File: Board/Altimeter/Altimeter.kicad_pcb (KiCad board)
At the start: 2 copper layers, 50 x 30 mm, 63 parts, among them J1 PWRIN, J2 STLink, J3 Micro_SD_Card_Det_Hirose_DM3AT, J4 GNSS, J5 RS485, J6 ReleaseSys, SW1 SW_RESET, U1 STM32L431RBTx, U2 LPS22HB_Module, U3 ST1480AxDR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

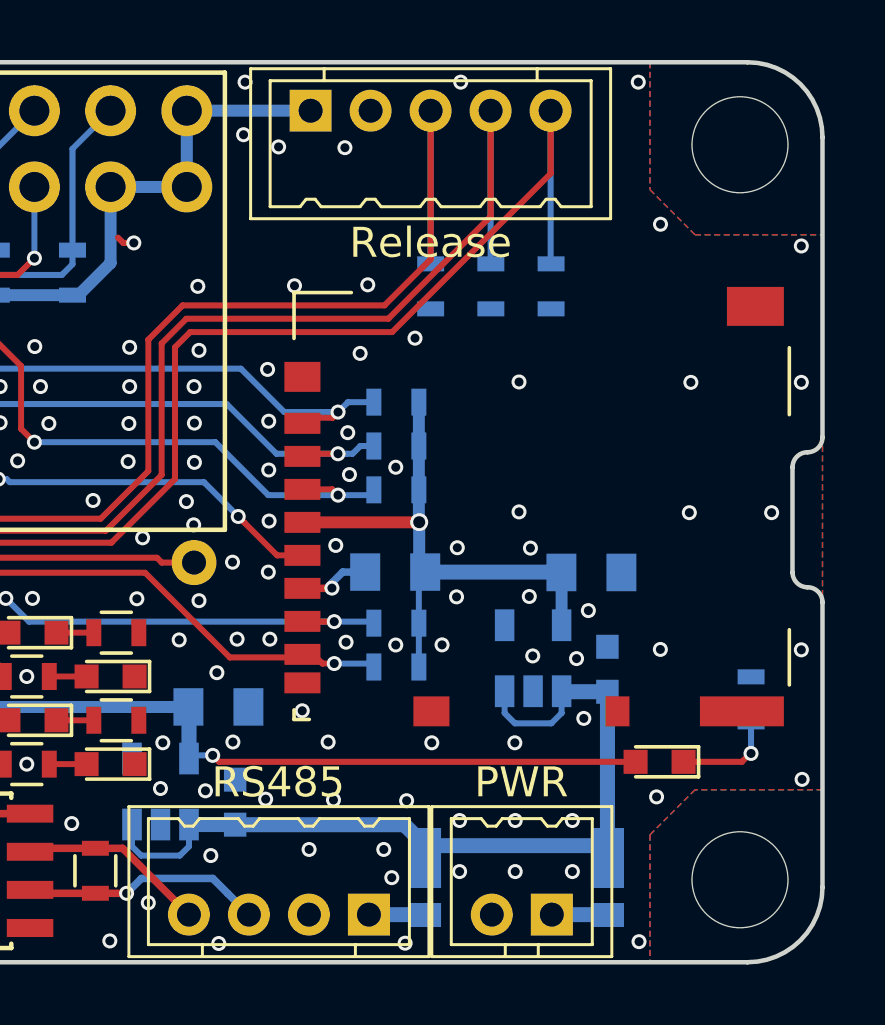
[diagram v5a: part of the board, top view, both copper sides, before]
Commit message: [Altimeter V1.2] Added another power input way at J6 and added a solder jumper to switch 3V Output / 6V Input.
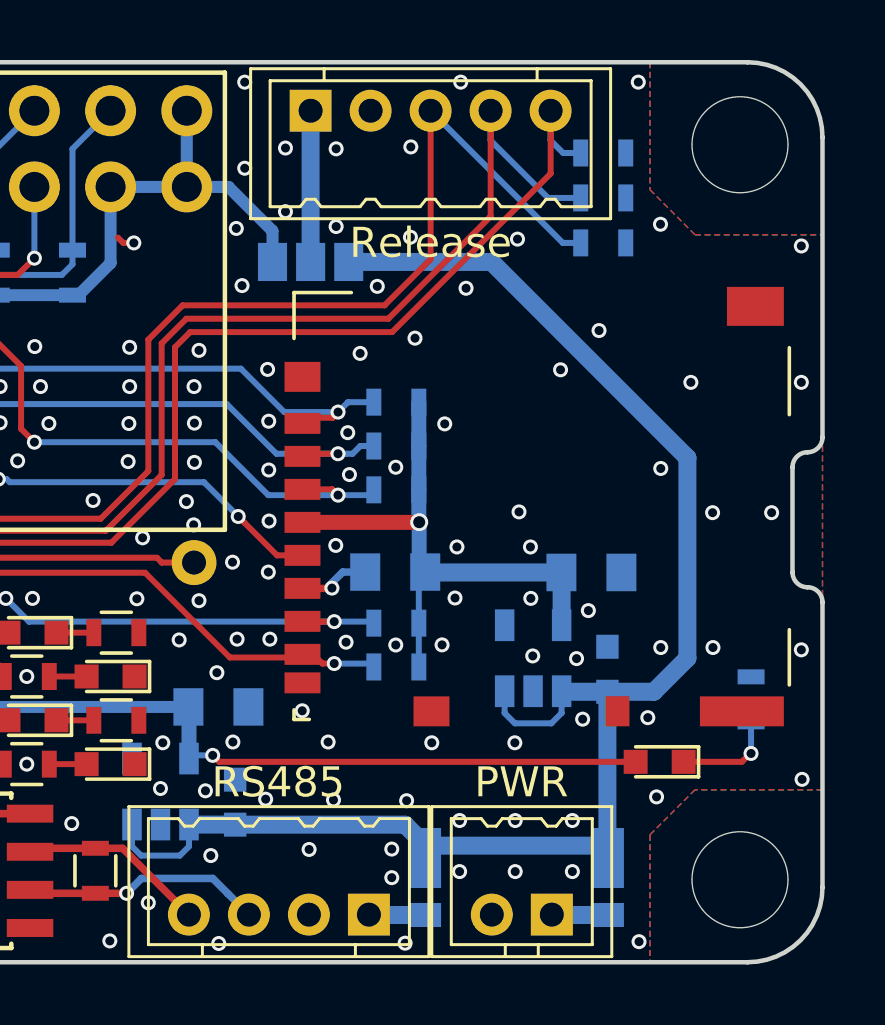
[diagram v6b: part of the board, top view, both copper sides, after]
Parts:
- added JP2: 6VIN/3.3VOUT, Connect:GS3, B.Cu at (157.9, 76.7)
- moved R16 5.93 mm to (167.7, 76.0), turned to 0 degrees
- moved R18 4.77 mm to (167.7, 73.0), turned to 0 degrees
- moved R17 4.77 mm to (167.7, 74.5), turned to 0 degrees
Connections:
- J6 pad 1: +3V3 -> Net-(J6-Pad1)
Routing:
- net +6V: track 29.3 -> 53.2 mm
- net Net-(J6-Pad1): track 0.00 -> 5.04 mm
- net /FLIGHTPIN: track 36.7 -> 33.8 mm
- net /TRIGGER: track 34.2 -> 35.9 mm
- net GND: vias 222 -> 233
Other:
- board text added: "3.3V Out"
- board text added: "6.0V In/3.3V Out"
- board text added: "6V"
- board text added: "Baro/GNSS Altimeter V1.2 @chromium_k 2018.12.10"
- board text added: "Input 3.0V-6.5V"
- board text removed: "+3.3V Out"
- board text removed: "+6V"
- board text removed: "Baro/GNSS Altimeter V1.1 @chromium_k 2018.08.10"
- board text removed: "Input 2.9V-6.5V"
